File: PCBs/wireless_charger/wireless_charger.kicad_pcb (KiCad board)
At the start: 4 copper layers, 65 x 30 mm, 97 parts, among them J1 Barrel_Jack_Switch, Q1 DMG7430LFG, Q2 DMG7430LFG, Q3 DMG7430LFG, Q4 DMG7430LFG, Q5 2N7002, Q6 SiA453EDJ, Q7 2N7002, Q8 2N7002, U1 P9242-RNDGI8

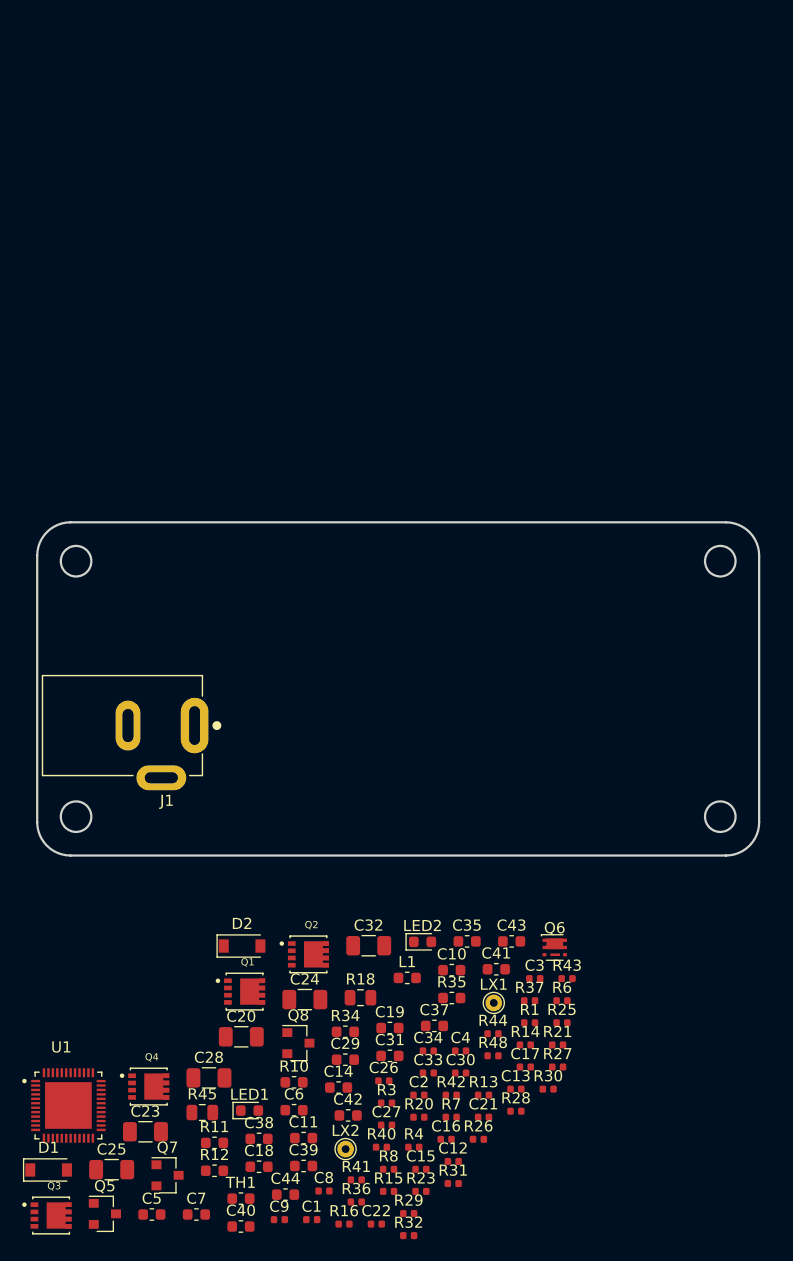
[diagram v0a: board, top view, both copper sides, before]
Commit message: completed the wireless charger PCB design as rev 0. bom is compiled
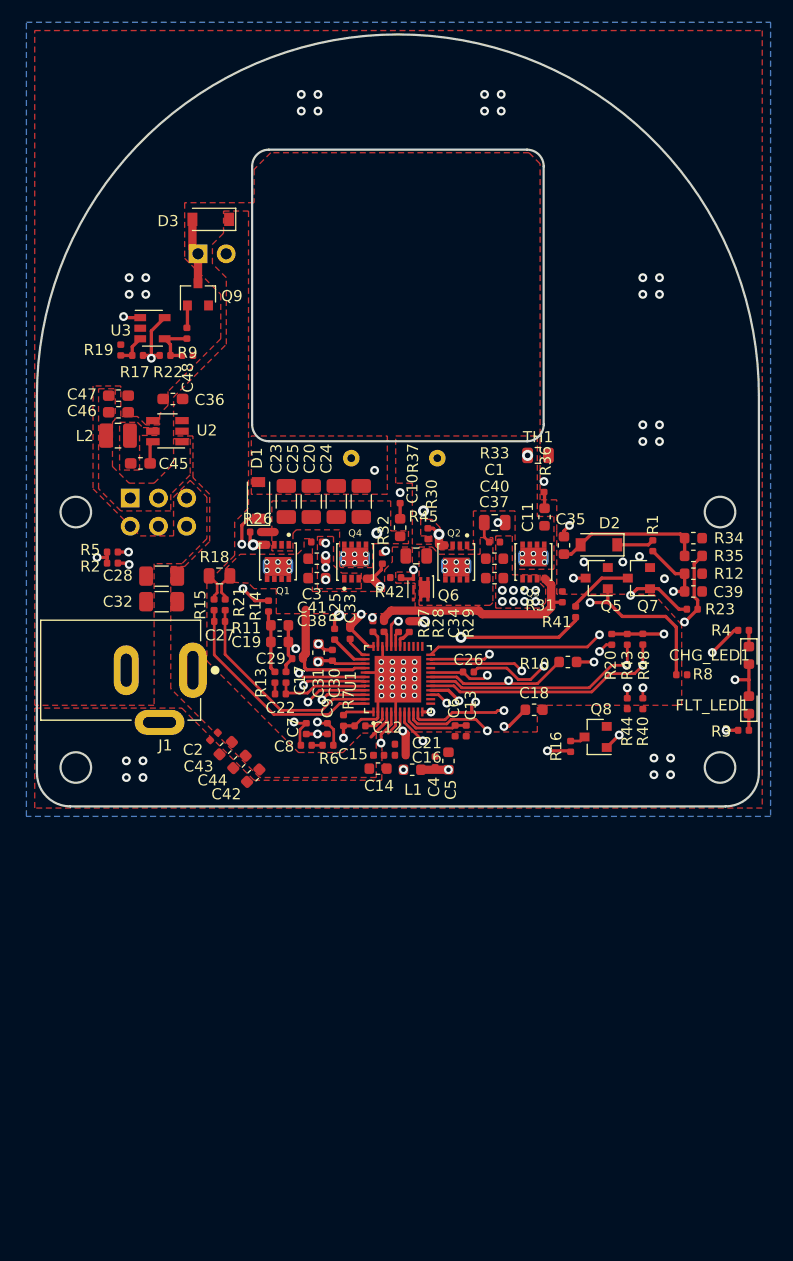
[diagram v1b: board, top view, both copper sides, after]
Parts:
- added C36: 10uF, Capacitor_SMD:C_0603_1608Metric_Pad1.05x0.95mm_HandSolder, F.Cu at (115.9, 72.4)
- added C45: 100nF, Capacitor_SMD:C_0603_1608Metric_Pad1.05x0.95mm_HandSolder, F.Cu at (113.0, 78.2)
- added C46: 10uF, Capacitor_SMD:C_0603_1608Metric_Pad1.05x0.95mm_HandSolder, F.Cu at (111.0, 73.6)
- added C47: 10uF, Capacitor_SMD:C_0603_1608Metric_Pad1.05x0.95mm_HandSolder, F.Cu at (111.0, 72.1)
- added C48: 15pF, Capacitor_SMD:C_0402_1005Metric, F.Cu at (117.3, 68.5)
- added D3: MBR0530, Diode_SMD:D_SOD-123, F.Cu at (119.3, 56.2)
- added Fan_12V1: Conn_01x02, Connector_PinHeader_2.54mm:PinHeader_1x02_P2.54mm_Vertical, B.Cu at (118.2, 59.4)
- added J2: Pi_Receiver, Connector_PinHeader_2.54mm:PinHeader_2x03_P2.54mm_Vertical, B.Cu at (112.1, 81.3)
- added L2: 4.7uH, Inductor_SMD:L_1008_2520Metric, F.Cu at (111.0, 75.7)
- added Q9: NTR4003N, Package_TO_SOT_SMD:SOT-23, F.Cu at (118.2, 63.0)
- added R17: 17.8, Resistor_SMD:R_0402_1005Metric, F.Cu at (112.8, 68.5)
- added R19: 10K, Resistor_SMD:R_0402_1005Metric, F.Cu at (111.2, 68.0)
- added R2: 10K, Resistor_SMD:R_0402_1005Metric, F.Cu at (110.5, 87.2)
- added R22: 10K, Resistor_SMD:R_0402_1005Metric, F.Cu at (115.2, 68.5)
- added R33: 3, Resistor_SMD:R_0805_2012Metric, F.Cu at (144.9, 83.5)
- added R5: 10K, Resistor_SMD:R_0402_1005Metric, F.Cu at (110.5, 86.2)
- added R9: 1K, Resistor_SMD:R_0402_1005Metric, F.Cu at (117.2, 66.5)
- added U2: AP63205, Package_TO_SOT_SMD:TSOT-23-6, F.Cu at (115.5, 75.3)
- added U3: LMV331, Package_TO_SOT_SMD:SOT-23-5, F.Cu at (114.1, 66.0)
- C29, C6, C7: footprint Capacitor_SMD:C_0603_1608Metric -> Capacitor_SMD:C_0402_1005Metric
- LX1, LX2: moved to B.Cu
- Q1, Q2, Q3, Q4: footprint Custom:TRANS_DMP3017SFGQ-7 -> Custom:TRANS_DMP3017SFGQ-7_b
- TH1: footprint Resistor_SMD:R_0603_1608Metric -> Resistor_SMD:R_0805_2012Metric
- U1: footprint QFN40P600X600X100-49N -> Custom:QFN40P600X600X100-49N
- moved Q3 73.1 mm to (148.4, 87.1), turned to 90 degrees
- moved Q5 72.4 mm to (154.1, 88.5), turned to 180 degrees
- moved TH1 72.1 mm to (148.8, 77.5)
- moved R12 68.9 mm to (162.8, 88.2)
- moved Q7 68.5 mm to (157.9, 88.5), turned to 180 degrees
- moved R36 66.6 mm to (149.3, 80.3), turned to 270 degrees
- moved C40 64.3 mm to (144.9, 86.8), turned to 180 degrees
- moved C1 63.2 mm to (144.9, 85.3), turned to 180 degrees
- moved D1 63.2 mm to (123.7, 81.5), turned to 90 degrees
- moved C25 62.8 mm to (128.4, 81.7), turned to 90 degrees
- moved C39 62.5 mm to (162.8, 89.8), turned to 180 degrees
- moved LX2 62.2 mm to (132.0, 77.8)
- moved R32 61.0 mm to (134.8, 86.8), turned to 270 degrees
- moved C11 60.0 mm to (149.4, 83.0), turned to 270 degrees
- moved R26 58.2 mm to (123.4, 84.4), turned to 180 degrees
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- renumbered LED2 to CHG_LED1, LED1 to FLT_LED1
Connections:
- net Net-(C11-Pad2) renamed /coil1
- net Net-(C20-Pad2) renamed /coil2
- net Net-(C26-Pad2) renamed /TS
- Q5 pad 3: Net-(C1-Pad2) -> Net-(Q5-Pad3)
- U1 pad 15: Net-(U1-Pad15) -> /SCL
- U1 pad 16: Net-(U1-Pad16) -> /SDA
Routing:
- net LDO33: track 0.00 -> 124.9 mm, vias 0 -> 7
- net /TS: track 0.00 -> 110.8 mm, vias 0 -> 4
- net /SDA: track 0.00 -> 47.4 mm, vias 0 -> 2
- net /SCL: track 0.00 -> 45.0 mm, vias 0 -> 2
- net Earth: track 0.00 -> 42.2 mm, vias 0 -> 72
- net Net-(R4-Pad1): track 0.00 -> 36.8 mm, vias 0 -> 3
- net Net-(R3-Pad1): track 0.00 -> 33.1 mm, vias 0 -> 2
- net Q_DRV1: track 0.00 -> 30.8 mm, vias 0 -> 2
- net VCOIL_OV: track 0.00 -> 27.2 mm, vias 0 -> 3
- net VCC_5V: track 0.00 -> 27.1 mm, vias 0 -> 3
- net Q_DRV2: track 0.00 -> 26.7 mm, vias 0 -> 2
- net /coil1: track 0.00 -> 25.1 mm, vias 0 -> 8
- net Net-(C10-Pad2): track 0.00 -> 25.1 mm, vias 0 -> 8
- net Net-(R40-Pad2): track 0.00 -> 25.1 mm, vias 0 -> 2
- net Net-(C29-Pad2): track 0.00 -> 25.0 mm, vias 0 -> 6
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- added copper zone on F.Cu, net +5V
- added copper zone on F.Cu, net /coil1
- added copper zone on F.Cu, net /coil2
- added copper zone on B.Cu, net Earth
- added copper zone on F.Cu, net Earth
- added copper zone on In1.Cu, net Earth
- added copper zone on In2.Cu, net Earth
- added copper zone on F.Cu, net Net-(C1-Pad2)
- added copper zone on F.Cu, net Net-(C10-Pad2)
- added copper zone on F.Cu, net Net-(C29-Pad2)
- added copper zone on F.Cu, net Net-(C45-Pad1)
- added copper zone on F.Cu, net VIN
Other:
- board size 65 x 30 mm -> 65 x 69.5 mm
- net class Chip added: clearance 0.125, trace_width 0.25, via_dia 0.8, via_drill 0.4
- net class Default: clearance 0.2 -> 0.125; trace_width 0.25 -> 0.3
- rule trace_clearance: 0.2 -> 0.125
- board text added: "12V"
- board text added: "GND 5V 5V"
- board text added: "NC SDA SCL"
